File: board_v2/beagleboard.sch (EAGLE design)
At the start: 40 parts, among them U1 DWM1000, X1 5566-2, X2 04-JST-B4B-XH-A

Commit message: pullups
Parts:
- added R16, R17: 10k, rcl:R-EU_R0805
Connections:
- net +5V: now also R16.2, R17.2
- net MLEN: now also R17.1
- net MREN: now also R16.1
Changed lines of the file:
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@@
 <part name="GND17" library="supply1" deviceset="GND" device=""/>
 <part name="GND18" library="supply1" deviceset="GND" device=""/>
+<part name="R16" library="rcl" deviceset="R-EU_" device="R0805" value="10k"/>
+<part name="R17" library="rcl" deviceset="R-EU_" device="R0805" value="10k"/>
 </parts>
 <sheets>
@@
 <instance part="P+4" gate="1" x="96.52" y="12.7"/>
 <instance part="+3V5" gate="G$1" x="60.96" y="81.28"/>
-<instance part="P+1" gate="1" x="-12.7" y="7.62"/>
-<instance part="P+9" gate="1" x="48.26" y="12.7"/>
+<instance part="P+1" gate="1" x="-12.7" y="15.24"/>
+<instance part="P+9" gate="1" x="48.26" y="15.24"/>
 <instance part="R1" gate="G$1" x="0" y="53.34" rot="R90"/>
 <instance part="R2" gate="G$1" x="5.08" y="38.1" rot="R90"/>
@@
 <instance part="GND17" gate="1" x="86.36" y="83.82"/>
 <instance part="GND18" gate="1" x="106.68" y="83.82"/>
+<instance part="R16" gate="G$1" x="58.42" y="5.08" rot="R90"/>
+<instance part="R17" gate="G$1" x="-2.54" y="5.08" rot="R90"/>
 </instances>
 <busses>
@@
 <wire x1="48.26" y1="-5.08" x2="48.26" y2="-2.54" width="0.1524" layer="91"/>
 <wire x1="48.26" y1="-2.54" x2="48.26" y2="10.16" width="0.1524" layer="91"/>
+<wire x1="48.26" y1="10.16" x2="48.26" y2="12.7" width="0.1524" layer="91"/>
 <wire x1="66.04" y1="-10.16" x2="48.26" y2="-10.16" width="0.1524" layer="91"/>
 <junction x="48.26" y="-10.16"/>
@@
 <wire x1="53.34" y1="-7.62" x2="48.26" y2="-7.62" width="0.1524" layer="91"/>
 <junction x="48.26" y="-7.62"/>
+<pinref part="R16" gate="G$1" pin="2"/>
+<wire x1="58.42" y1="10.16" x2="48.26" y2="10.16" width="0.1524" layer="91"/>
+<junction x="48.26" y="10.16"/>
 </segment>
 <segment>
@@
 <wire x1="-12.7" y1="-7.62" x2="-12.7" y2="-5.08" width="0.1524" layer="91"/>
 <wire x1="-12.7" y1="-5.08" x2="-12.7" y2="-2.54" width="0.1524" layer="91"/>
-<wire x1="-12.7" y1="-2.54" x2="-12.7" y2="5.08" width="0.1524" layer="91"/>
+<wire x1="-12.7" y1="-2.54" x2="-12.7" y2="10.16" width="0.1524" layer="91"/>
+<wire x1="-12.7" y1="10.16" x2="-12.7" y2="12.7" width="0.1524" layer="91"/>
 <wire x1="-7.62" y1="-2.54" x2="-12.7" y2="-2.54" width="0.1524" layer="91"/>
 <junction x="-12.7" y="-2.54"/>
@@
 <wire x1="-7.62" y1="-7.62" x2="-12.7" y2="-7.62" width="0.1524" layer="91"/>
 <junction x="-12.7" y="-7.62"/>
+<pinref part="R17" gate="G$1" pin="2"/>
+<wire x1="-2.54" y1="10.16" x2="-12.7" y2="10.16" width="0.1524" layer="91"/>
+<junction x="-12.7" y="10.16"/>
 </segment>
 </net>
@@
 <segment>
 <pinref part="MOTORL" gate="A" pin="1"/>
-<wire x1="5.08" y1="0" x2="-5.08" y2="0" width="0.1524" layer="91"/>
+<wire x1="5.08" y1="0" x2="-2.54" y2="0" width="0.1524" layer="91"/>
 <label x="-5.08" y="0" size="1.016" layer="95" rot="R180" xref="yes"/>
+<pinref part="R17" gate="G$1" pin="1"/>
+<wire x1="-2.54" y1="0" x2="-5.08" y2="0" width="0.1524" layer="91"/>
+<junction x="-2.54" y="0"/>
 </segment>
 <segment>
@@
 <segment>
 <pinref part="MOTOTR" gate="A" pin="1"/>
-<wire x1="66.04" y1="0" x2="55.88" y2="0" width="0.1524" layer="91"/>
+<wire x1="66.04" y1="0" x2="58.42" y2="0" width="0.1524" layer="91"/>
 <label x="55.88" y="0" size="1.016" layer="95" rot="R180" xref="yes"/>
-</segment>
-<segment>
+<pinref part="R16" gate="G$1" pin="1"/>
+<wire x1="58.42" y1="0" x2="55.88" y2="0" width="0.1524" layer="91"/>
+<junction x="58.42" y="0"/>
+</segment>
+<segment>

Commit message: values
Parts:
- R10, R12, R14: value (none) -> 1,1k
- R11, R13, R15: value (none) -> 2k
- R4, R5, R6: value (none) -> 1k
- R7, R8, R9: value (none) -> 1,5k
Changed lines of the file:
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@@
 <part name="X2" library="bt_con-jst-xh" deviceset="04-JST" device="-B4B-XH-A"/>
 <part name="GND13" library="supply1" deviceset="GND" device=""/>
-<part name="R4" library="rcl" deviceset="R-EU_" device="R0805"/>
-<part name="R5" library="rcl" deviceset="R-EU_" device="R0805"/>
-<part name="R6" library="rcl" deviceset="R-EU_" device="R0805"/>
-<part name="R7" library="rcl" deviceset="R-EU_" device="R0805"/>
-<part name="R8" library="rcl" deviceset="R-EU_" device="R0805"/>
-<part name="R9" library="rcl" deviceset="R-EU_" device="R0805"/>
+<part name="R4" library="rcl" deviceset="R-EU_" device="R0805" value="1k"/>
+<part name="R5" library="rcl" deviceset="R-EU_" device="R0805" value="1k"/>
+<part name="R6" library="rcl" deviceset="R-EU_" device="R0805" value="1k"/>
+<part name="R7" library="rcl" deviceset="R-EU_" device="R0805" value="1,5k"/>
+<part name="R8" library="rcl" deviceset="R-EU_" device="R0805" value="1,5k"/>
+<part name="R9" library="rcl" deviceset="R-EU_" device="R0805" value="1,5k"/>
 <part name="P+8" library="supply1" deviceset="+5V" device=""/>
 <part name="SENS1" library="libsjst_eph" deviceset="4PIN" device=""/>
@@
 <part name="SJ5" library="jumper" deviceset="SJ" device=""/>
 <part name="SJ6" library="jumper" deviceset="SJ" device=""/>
-<part name="R10" library="rcl" deviceset="R-EU_" device="R0805"/>
-<part name="R11" library="rcl" deviceset="R-EU_" device="R0805"/>
-<part name="R12" library="rcl" deviceset="R-EU_" device="R0805"/>
-<part name="R13" library="rcl" deviceset="R-EU_" device="R0805"/>
-<part name="R14" library="rcl" deviceset="R-EU_" device="R0805"/>
-<part name="R15" library="rcl" deviceset="R-EU_" device="R0805"/>
+<part name="R10" library="rcl" deviceset="R-EU_" device="R0805" value="1,1k"/>
+<part name="R11" library="rcl" deviceset="R-EU_" device="R0805" value="2k"/>
+<part name="R12" library="rcl" deviceset="R-EU_" device="R0805" value="1,1k"/>
+<part name="R13" library="rcl" deviceset="R-EU_" device="R0805" value="2k"/>
+<part name="R14" library="rcl" deviceset="R-EU_" device="R0805" value="1,1k"/>
+<part name="R15" library="rcl" deviceset="R-EU_" device="R0805" value="2k"/>
 <part name="GND15" library="supply1" deviceset="GND" device=""/>
 <part name="GND17" library="supply1" deviceset="GND" device=""/>

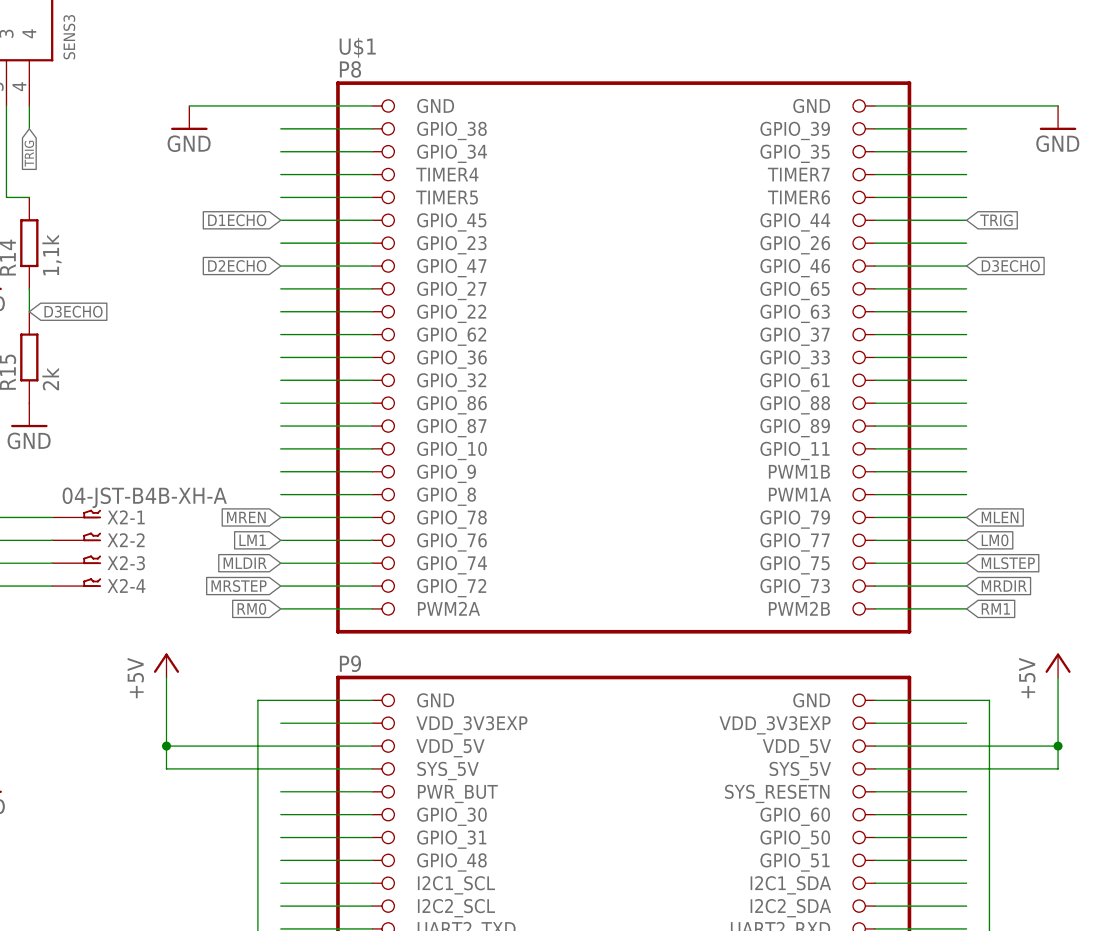
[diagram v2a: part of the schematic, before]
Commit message: right sonar wires
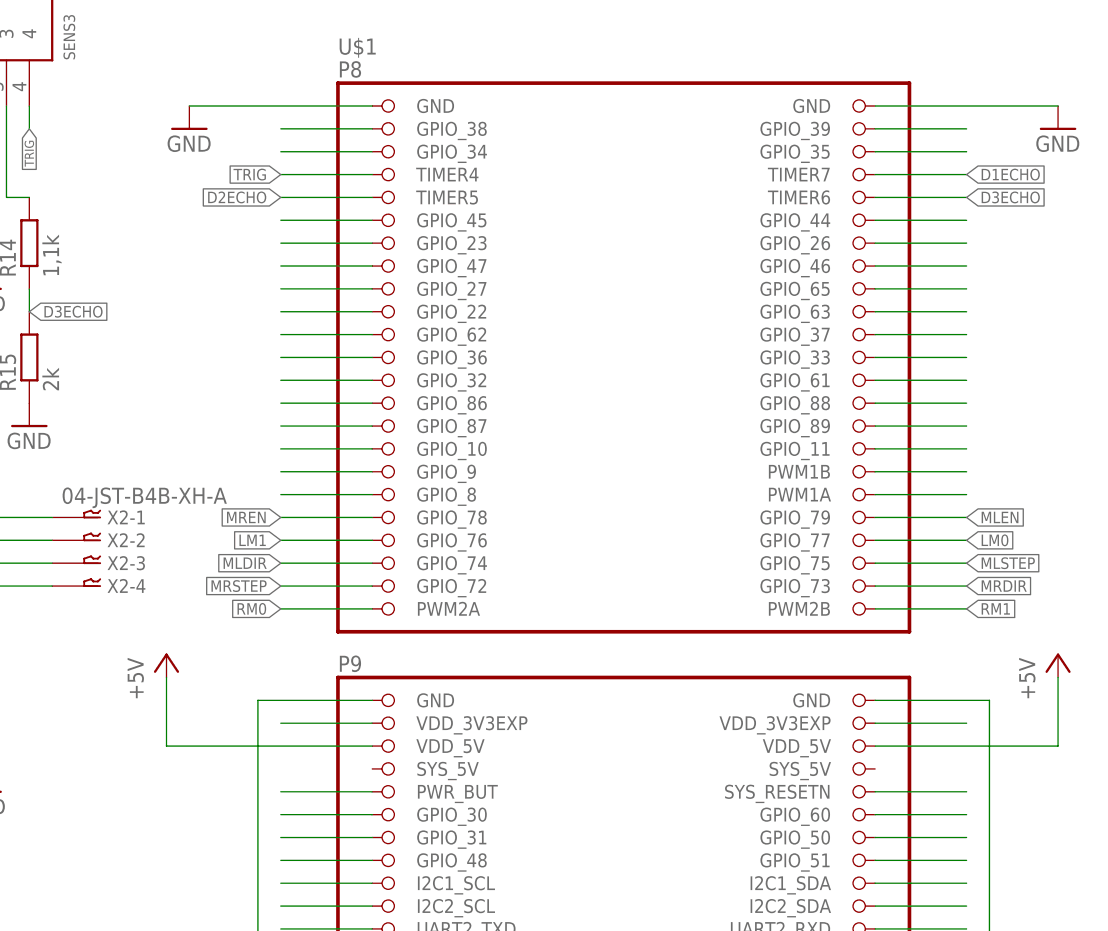
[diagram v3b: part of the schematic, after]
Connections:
- removed net N$42: U$1.TIMER5
- new net N$26: U$1.GPIO_47
- net +5V: no longer U$1.SYS_5V@1, U$1.SYS_5V@2
- net D1ECHO: now also U$1.TIMER7; no longer U$1.GPIO_45
- net D2ECHO: now also U$1.TIMER5; no longer U$1.GPIO_47
- net D3ECHO: now also U$1.TIMER6; no longer U$1.GPIO_46
- net N$20: now also U$1.GPIO_44; no longer U$1.TIMER4
- net N$22: now also U$1.GPIO_46; no longer U$1.TIMER7
- net N$23: now also U$1.GPIO_45; no longer U$1.TIMER6
- net TRIG: now also U$1.TIMER4; no longer U$1.GPIO_44
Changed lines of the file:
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@@
 <pinref part="U$1" gate="G$1" pin="VDD_5V@2"/>
 <wire x1="200.66" y1="48.26" x2="220.98" y2="48.26" width="0.1524" layer="91"/>
-<pinref part="U$1" gate="G$1" pin="SYS_5V@2"/>
-<wire x1="200.66" y1="45.72" x2="220.98" y2="45.72" width="0.1524" layer="91"/>
-<wire x1="220.98" y1="45.72" x2="220.98" y2="48.26" width="0.1524" layer="91"/>
-<junction x="220.98" y="48.26"/>
 </segment>
 <segment>
 <pinref part="U$1" gate="G$1" pin="VDD_5V@1"/>
-<pinref part="U$1" gate="G$1" pin="SYS_5V@1"/>
-<wire x1="144.78" y1="45.72" x2="121.92" y2="45.72" width="0.1524" layer="91"/>
-<wire x1="121.92" y1="45.72" x2="121.92" y2="48.26" width="0.1524" layer="91"/>
 <wire x1="121.92" y1="48.26" x2="121.92" y2="55.88" width="0.1524" layer="91"/>
 <wire x1="144.78" y1="48.26" x2="121.92" y2="48.26" width="0.1524" layer="91"/>
-<junction x="121.92" y="48.26"/>
 <pinref part="P+6" gate="1" pin="+5V"/>
 </segment>
@@
 </segment>
 </net>
-<net name="N$22" class="0">
-<segment>
-<pinref part="U$1" gate="G$1" pin="TIMER7"/>
-<wire x1="200.66" y1="111.76" x2="210.82" y2="111.76" width="0.1524" layer="91"/>
-</segment>
-</net>
-<net name="N$23" class="0">
-<segment>
-<pinref part="U$1" gate="G$1" pin="TIMER6"/>
-<wire x1="200.66" y1="109.22" x2="210.82" y2="109.22" width="0.1524" layer="91"/>
-</segment>
-</net>
 <net name="N$25" class="0">
 <segment>
@@
 </segment>
 <segment>
-<pinref part="U$1" gate="G$1" pin="GPIO_44"/>
-<wire x1="200.66" y1="106.68" x2="210.82" y2="106.68" width="0.1524" layer="91"/>
-<label x="210.82" y="106.68" size="1.27" layer="95" xref="yes"/>
+<pinref part="U$1" gate="G$1" pin="TIMER4"/>
+<wire x1="144.78" y1="111.76" x2="134.62" y2="111.76" width="0.1524" layer="91"/>
+<label x="134.62" y="111.76" size="1.27" layer="95" rot="R180" xref="yes"/>
 </segment>
 </net>
@@
 </segment>
 </net>
-<net name="N$20" class="0">
-<segment>
-<pinref part="U$1" gate="G$1" pin="TIMER4"/>
-<wire x1="144.78" y1="111.76" x2="134.62" y2="111.76" width="0.1524" layer="91"/>
-</segment>
-</net>
-<net name="N$42" class="0">
-<segment>
-<pinref part="U$1" gate="G$1" pin="TIMER5"/>
-<wire x1="144.78" y1="109.22" x2="134.62" y2="109.22" width="0.1524" layer="91"/>
-</segment>
-</net>
 <net name="N$44" class="0">
 <segment>
@@
 </segment>
 <segment>
-<pinref part="U$1" gate="G$1" pin="GPIO_45"/>
-<wire x1="144.78" y1="106.68" x2="134.62" y2="106.68" width="0.1524" layer="91"/>
-<label x="134.62" y="106.68" size="1.27" layer="95" rot="R180" xref="yes"/>
+<pinref part="U$1" gate="G$1" pin="TIMER7"/>
+<wire x1="200.66" y1="111.76" x2="210.82" y2="111.76" width="0.1524" layer="91"/>
+<label x="210.82" y="111.76" size="1.27" layer="95" xref="yes"/>
 </segment>
 </net>
@@
 </segment>
 <segment>
-<pinref part="U$1" gate="G$1" pin="GPIO_47"/>
-<wire x1="144.78" y1="101.6" x2="134.62" y2="101.6" width="0.1524" layer="91"/>
-<label x="134.62" y="101.6" size="1.27" layer="95" rot="R180" xref="yes"/>
+<pinref part="U$1" gate="G$1" pin="TIMER5"/>
+<wire x1="144.78" y1="109.22" x2="134.62" y2="109.22" width="0.1524" layer="91"/>
+<label x="134.62" y="109.22" size="1.27" layer="95" rot="R180" xref="yes"/>
 </segment>
 </net>
@@
 </segment>
 <segment>
+<pinref part="U$1" gate="G$1" pin="TIMER6"/>
+<wire x1="200.66" y1="109.22" x2="210.82" y2="109.22" width="0.1524" layer="91"/>
+<label x="210.82" y="109.22" size="1.27" layer="95" xref="yes"/>
+</segment>
+</net>
+<net name="N$77" class="0">
+<segment>
+<pinref part="U$1" gate="G$1" pin="GPIO_7"/>
+<wire x1="200.66" y1="2.54" x2="210.82" y2="2.54" width="0.1524" layer="91"/>
+</segment>
+</net>
+<net name="N$79" class="0">
+<segment>
+<pinref part="U$1" gate="G$1" pin="I2C1_SCL"/>
+<wire x1="144.78" y1="33.02" x2="134.62" y2="33.02" width="0.1524" layer="91"/>
+</segment>
+</net>
+<net name="N$20" class="0">
+<segment>
+<pinref part="U$1" gate="G$1" pin="GPIO_44"/>
+<wire x1="200.66" y1="106.68" x2="210.82" y2="106.68" width="0.1524" layer="91"/>
+</segment>
+</net>
+<net name="N$22" class="0">
+<segment>
 <pinref part="U$1" gate="G$1" pin="GPIO_46"/>
 <wire x1="200.66" y1="101.6" x2="210.82" y2="101.6" width="0.1524" layer="91"/>
-<label x="210.82" y="101.6" size="1.27" layer="95" xref="yes"/>
-</segment>
-</net>
-<net name="N$77" class="0">
-<segment>
-<pinref part="U$1" gate="G$1" pin="GPIO_7"/>
-<wire x1="200.66" y1="2.54" x2="210.82" y2="2.54" width="0.1524" layer="91"/>
-</segment>
-</net>
-<net name="N$79" class="0">
-<segment>
-<pinref part="U$1" gate="G$1" pin="I2C1_SCL"/>
-<wire x1="144.78" y1="33.02" x2="134.62" y2="33.02" width="0.1524" layer="91"/>
-</segment>
-</net>
+</segment>
+</net>
+<net name="N$23" class="0">
+<segment>
+<pinref part="U$1" gate="G$1" pin="GPIO_45"/>
+<wire x1="144.78" y1="106.68" x2="134.62" y2="106.68" width="0.1524" layer="91"/>
+</segment>
+</net>
+<net name="N$26" class="0">
+<segment>
+<pinref part="U$1" gate="G$1" pin="GPIO_47"/>
+<wire x1="144.78" y1="101.6" x2="134.62" y2="101.6" width="0.1524" layer="91"/>
+</segment>
+</net>
